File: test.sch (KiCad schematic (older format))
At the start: 187 parts, among them J1 GNIAZDO_MODULU_1, J2 GNIAZDO_MODULU_2, J3 GNIAZDO_MODULU_3, J4 GNIAZDO_MODULU_4, J5 GNIAZDO_MODULU_5, J6 GNIAZDO_MODULU_6, J7 microSD, P1 Gniazdo akumulatora, P2 Gniazdo akumulatora, P3 Gniazdo programatora SWD, T1 IRLML6401, T10 BSS138, T11 BSS138, T12 BSS138, T13 BSS138, T14 FDV304P, T2 IRLML6401, T3 IRLML6401, T4 IRLML6401, T5 IRLML6401, T6 IRLML6401, T7 BSS138, T8 BSS138, T9 BSS138, U1 MCP1755T-3302E/DC, U10 MCP1755T-3302E/DC, U11 MIC29302, U12 TPS3823, U13 DHT22, U14 DS3231SN, U15 M590E, U16 S25FL1275ABMGI101, U17 ESP-07, U18 SIMHOLDER, U19 MAX3485, U2 MCP1755T-3302E/DC, U3 MCP1755T-3302E/DC, U4 MCP1755T-3302E/DC, U5 MCP1755T-3302E/DC, U6 MCP1755T-3302E/DC, U7 74LVX373M, U8 74LVX373M, U9 STM32F103C8, Y1 32768, Y2 14.7456 MHz

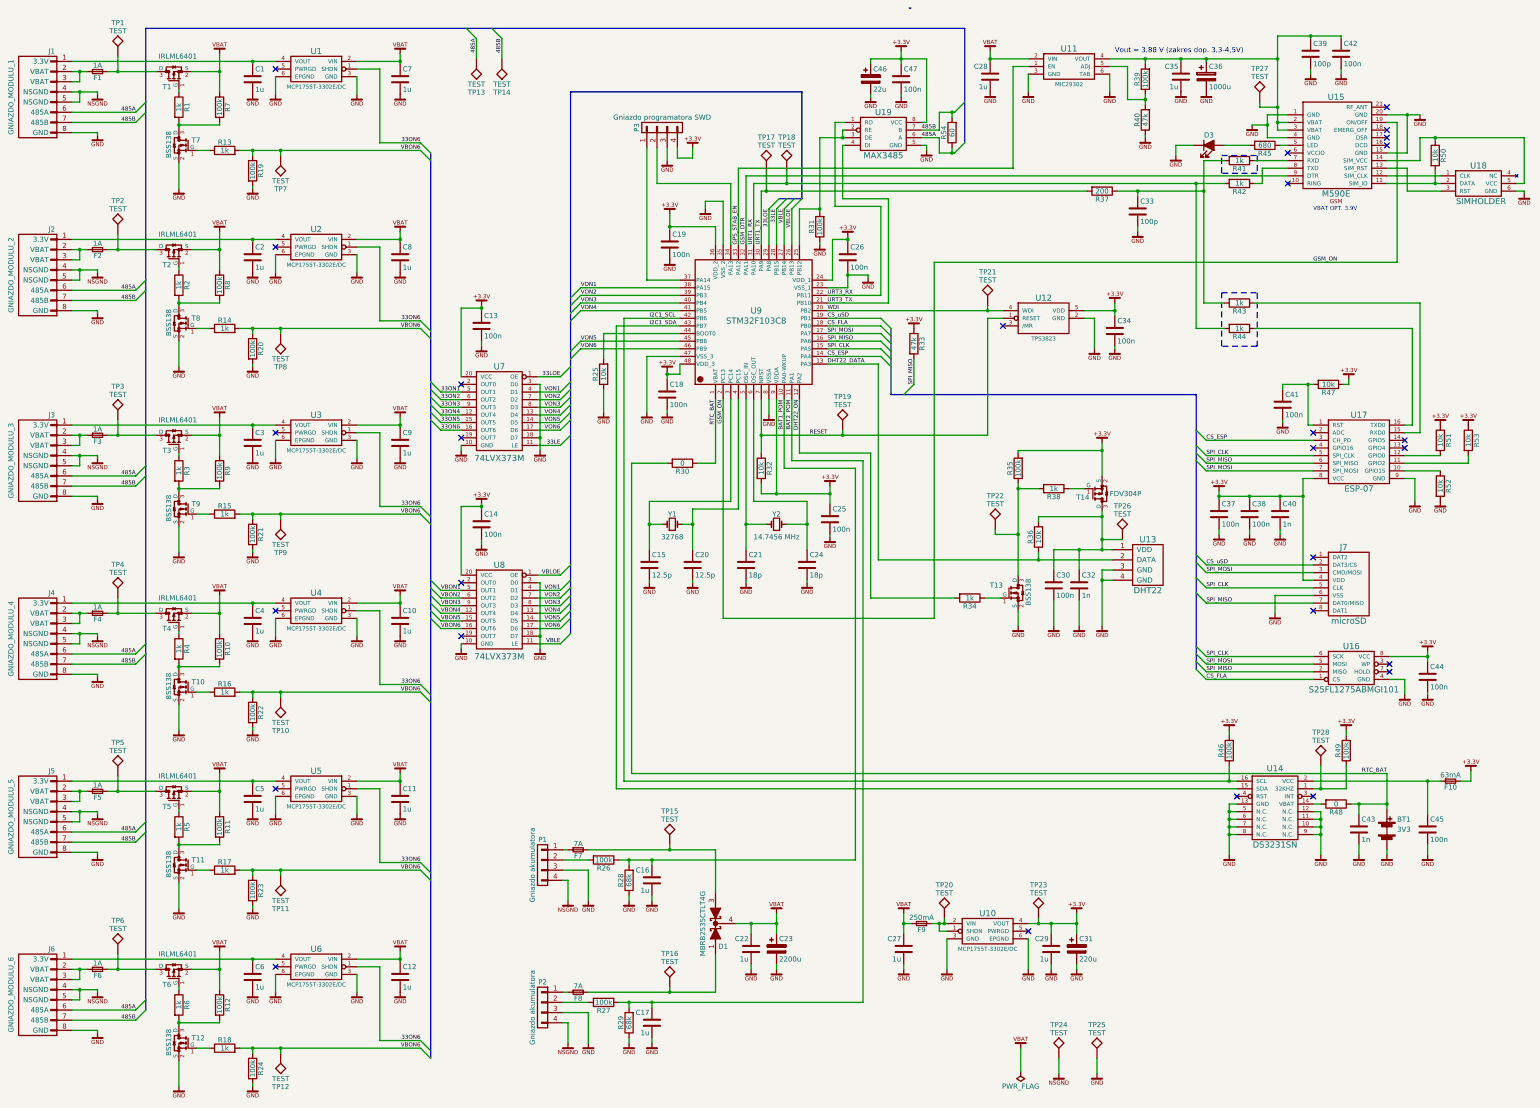
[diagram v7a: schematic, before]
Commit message: zmiana procesora na STM32L051R8
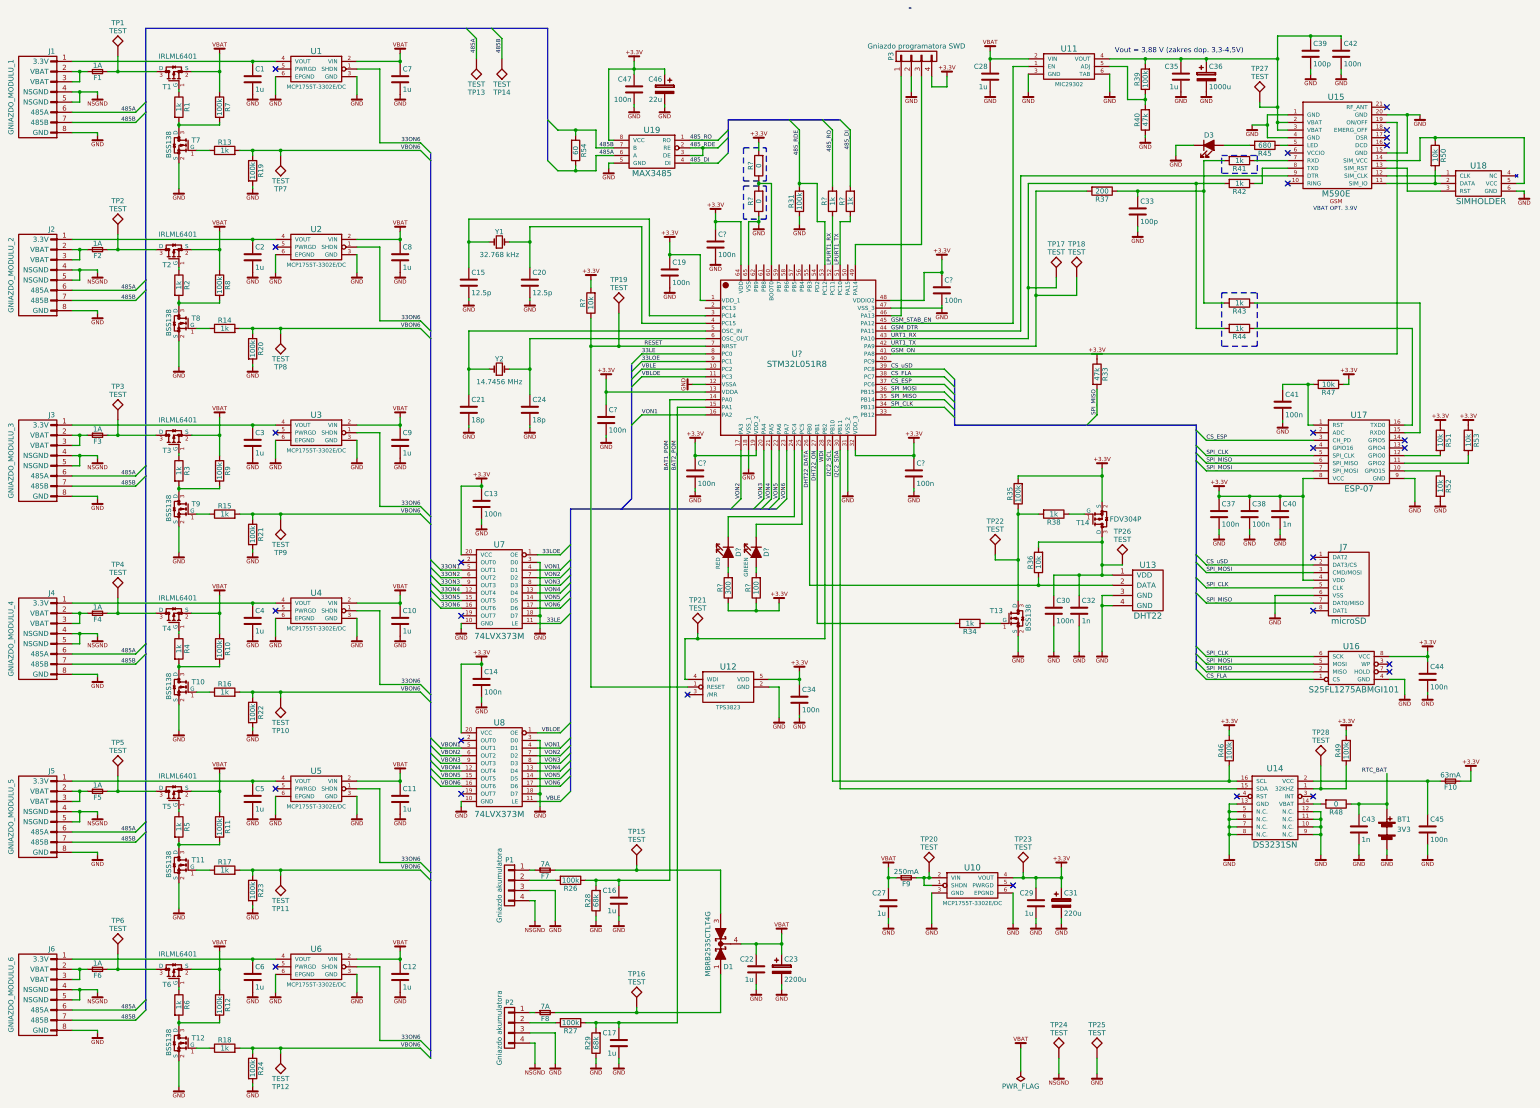
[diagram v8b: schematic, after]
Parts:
- removed C18, C25, C26: 100n, Capacitors_SMD:C_0603, symbol C
- removed R25, R32: 10k, Resistors_SMD:R_0603, symbol R
- removed R30: 0, Resistors_SMD:R_0603, symbol R
- removed U9: STM32F103C8, Housings_QFP:LQFP-48_7x7mm_Pitch0.5mm, symbol STM32F103C8
- added C? (x5): 100n, Capacitors_SMD:C_0603, symbol C
- added D?: RED, symbol LED
- added D?: GREEN, symbol LED
- added R?: 10k, Resistors_SMD:R_0603, symbol R
- added R? (x2): 1k, Resistors_SMD:R_0603, symbol R
- added R? (x2): 0, Resistors_SMD:R_0603, symbol R
- added R?: 100, Resistors_SMD:R_0603, symbol R
- added R?: 300, Resistors_SMD:R_0603, symbol R
- added U?: STM32L051R8, symbol STM32L051R8
- Y1: value 32768 -> 32.768 kHz
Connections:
- net 33LE: now also U?.8 (PC0)
- net 33LOE: now also U?.9 (PC1)
- net BAT1_POM: now also U?.14 (PA0)
- net BAT2_POM: now also U?.15 (PA1)
- net CS_ESP: now also U?.37 (PC6)
- net CS_FLA: now also U?.38 (PC7)
- net CS_uSD: now also U?.39 (PC8)
- net DHT22_DATA: now also U?.26 (PB0)
- net DHT22_ON: now also U?.27 (PB1)
- net GSM_DTR: now also U?.44 (PA11)
- net GSM_ON: now also U?.41 (PA8)
- net RESET: now also R?.1, U?.7 (NRST)
- net SPI_CLK: now also U?.34 (PB13)
- net SPI_MISO: now also U?.35 (PB14)
- net SPI_MOSI: now also U?.36 (PB15)
- net URT1_RX: now also TP17.1, U?.43 (PA10); no longer TP18.1
- net URT1_TX: now also TP18.1, U?.42 (PA9); no longer TP17.1
- net VBLE: now also U?.10 (PC2)
- net VBLOE: now also U?.11 (PC3)
- net VON1: now also U?.16 (PA2)
- net VON2: now also U?.17 (PA3)
- net VON3: now also U?.20 (PA4)
- net VON4: now also U?.21 (PA5)
- net VON5: now also U?.22 (PA6)
- net VON6: now also U?.23 (PA7)
- net WDI: now also U?.28 (PB2)
- net 485_RDE: now reaches R31.2, U19.2 (RE), U19.3 (DE)
- net 485_RDE: now also U?.53 (PC12)
- net at C15.1, Y1.1: now also U?.3 (PC14)
- net at C19.1: now also U?.1 (VDD_1)
- net at P3.1 (P1): now also U?.46 (PA13)
- net at C20.1, Y1.2: now also U?.4 (PC15)
- net at C21.1, Y2.1: now also U?.5 (OSC_IN)
- net at C24.1, Y2.2: now also U?.6 (OSC_OUT)
- net at P3.3 (P3): now also U?.49 (PA14)
- net GPS_STAB_EN renamed GSM_STAB_EN
- net GSM_STAB_EN: now also U?.45 (PA12)
- net I2C1_SCL renamed I2C2_SCL
- net I2C2_SCL: now also U?.29 (PB10)
- net I2C1_SDA renamed I2C2_SDA
- net I2C2_SDA: now also U?.30 (PB11)
- net URT3_RX renamed 485_RO
- net 485_RO: now also R?.2
- net URT3_TX renamed 485_DI
- net 485_DI: now also R?.2
- new net: C?.1, U?.13 (VDDA)
- new net: C?.1, U?.19 (VDD_2)
- new net: D?.1 (K), U?.24 (PC4)
- new net: D?.1 (K), U?.25 (PC5)
- new net: C?.1, U?.32 (VDD_3)
- new net: C?.2, U?.47 (VSS_3)
- new net: C?.1, U?.48 (VDDIO2)
- new net: R?.1, R?.2, U?.60 (BOOT0)
- new net: C?.1, U?.64 (VDD)
- new net: R?.1, U?.65 (VSS)
- new net: D?.2 (A), R?.2 (x2)
- new net: R?.1, R?.1
- new net LPURT1_RX: R?.1, U?.52 (PC11)
- new net LPURT1_TX: R?.1, U?.51 (PC10)
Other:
- moved on the sheet: C13, C14, C15, C16, C17, C19, C20, C21, C22, C23, C24, C27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
